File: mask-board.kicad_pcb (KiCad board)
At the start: 2 copper layers, 56.5 x 41.9 mm, 58 parts, among them J1 SWIM Connector, J2 I2C Breakout, M1 Fan_3pin, M2 Fan_3pin, M3 Motor_DC, Q1 2N7000, Q2 2N7000, Q3 2N7000, Q4 2N7000, SW1 SW_Push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

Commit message: Update to V3
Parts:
- D2, D3, D4: value D_Schottky -> PMEG4010ER; footprint Package_TO_SOT_SMD:SOT-23-3 -> Diode_SMD:Nexperia_CFP3_SOD-123W
- M1, M2: footprint Connector_PinHeader_2.54mm:PinHeader_1x03_P2.54mm_Vertical -> footprints:JST-XH-3-pin
- M3: footprint Connector_PinHeader_2.54mm:PinHeader_1x02_P2.54mm_Vertical -> footprints:JST-XH-2-pin
- Q1, Q2, Q3, Q4: value 2N7000 -> DMN10H220L; footprint Package_TO_SOT_THT:TO-92_Inline -> Package_TO_SOT_SMD:SOT-23
- moved Q2 9.75 mm to (166.4, 99.4), turned to 0 degrees
- moved R11 7.41 mm to (160.3, 104.1), turned to 90 degrees
- moved C17 5.15 mm to (170.5, 104.1)
- moved C18 5.15 mm to (166.7, 104.1)
- moved C19 5.15 mm to (168.6, 104.1)
- moved M3 4.74 mm to (174.0, 102.8), turned to 90 degrees
- moved M2 4.13 mm to (174.0, 93.0), turned to 90 degrees
- moved R10 3.62 mm to (162.2, 104.1), turned to 90 degrees
- moved M1 3.18 mm to (174.0, 81.9), turned to 90 degrees
- moved Q4 2.53 mm to (166.0, 89.2), turned to 0 degrees
- moved R14 1.94 mm to (163.8, 93.2)
- moved R15 1.94 mm to (165.7, 93.2)
- moved Q1 1.44 mm to (154.6, 96.5), turned to 0 degrees
- moved Q3 0.95 mm to (164.8, 80.3), turned to 0 degrees
- moved D2 0.55 mm to (169.9, 98.9), turned to -90 degrees
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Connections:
- Q1 pad 1: GND -> Net-(Q1-G)
- Q1 pad 2: Net-(Q1-G) -> GND
- Q2 pad 1: GND -> Net-(Q2-G)
- Q2 pad 2: Net-(Q2-G) -> GND
- Q3 pad 1: GND -> Net-(Q3-G)
- Q3 pad 2: Net-(Q3-G) -> GND
- Q4 pad 1: GND -> Net-(Q4-G)
- Q4 pad 2: Net-(Q4-G) -> GND
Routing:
- net ERM_MOTOR: track 20.1 -> 14.1 mm
- net Net-(BZ1--): track 8.40 -> 14.0 mm, vias 0 -> 1
- net +3V3: track 157.4 -> 162.9 mm
- net +5V: track 71.3 -> 74.6 mm
- net Net-(Q2-G): track 5.01 -> 7.10 mm
- net FAN_2: track 18.2 -> 20.2 mm
- net Net-(D4-A): track 9.43 -> 7.82 mm
- net Net-(D2-A): track 10.2 -> 8.65 mm
- net Net-(Q1-G): track 4.65 -> 5.88 mm
- net Net-(M2-Tacho): track 2.99 -> 3.63 mm
- net Net-(Q4-G): track 5.11 -> 4.59 mm
- net GND: track 77.4 -> 77.8 mm, vias 5 -> 8
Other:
- board size 56.5 x 41.9 mm -> 61 x 41.9 mm

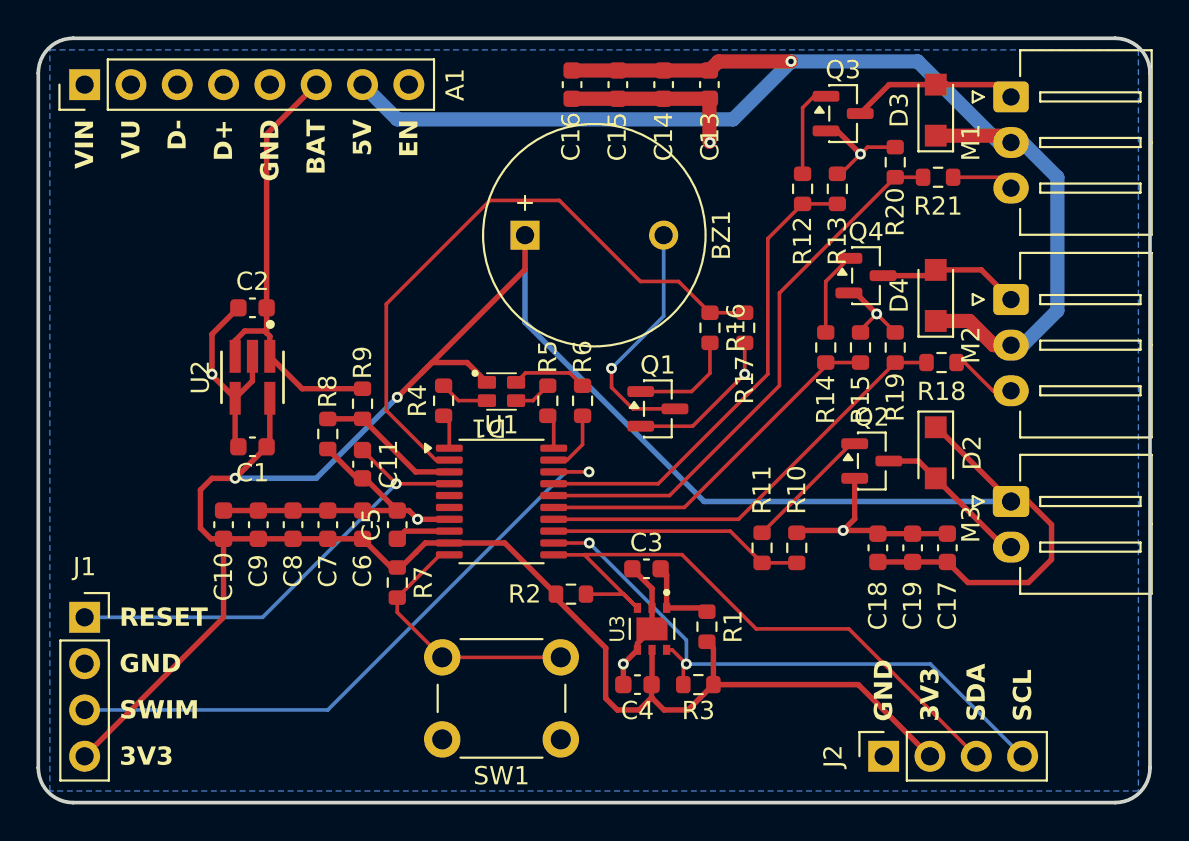
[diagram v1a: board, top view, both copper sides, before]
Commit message: Update to V4; Add quarter for scale in 3D model
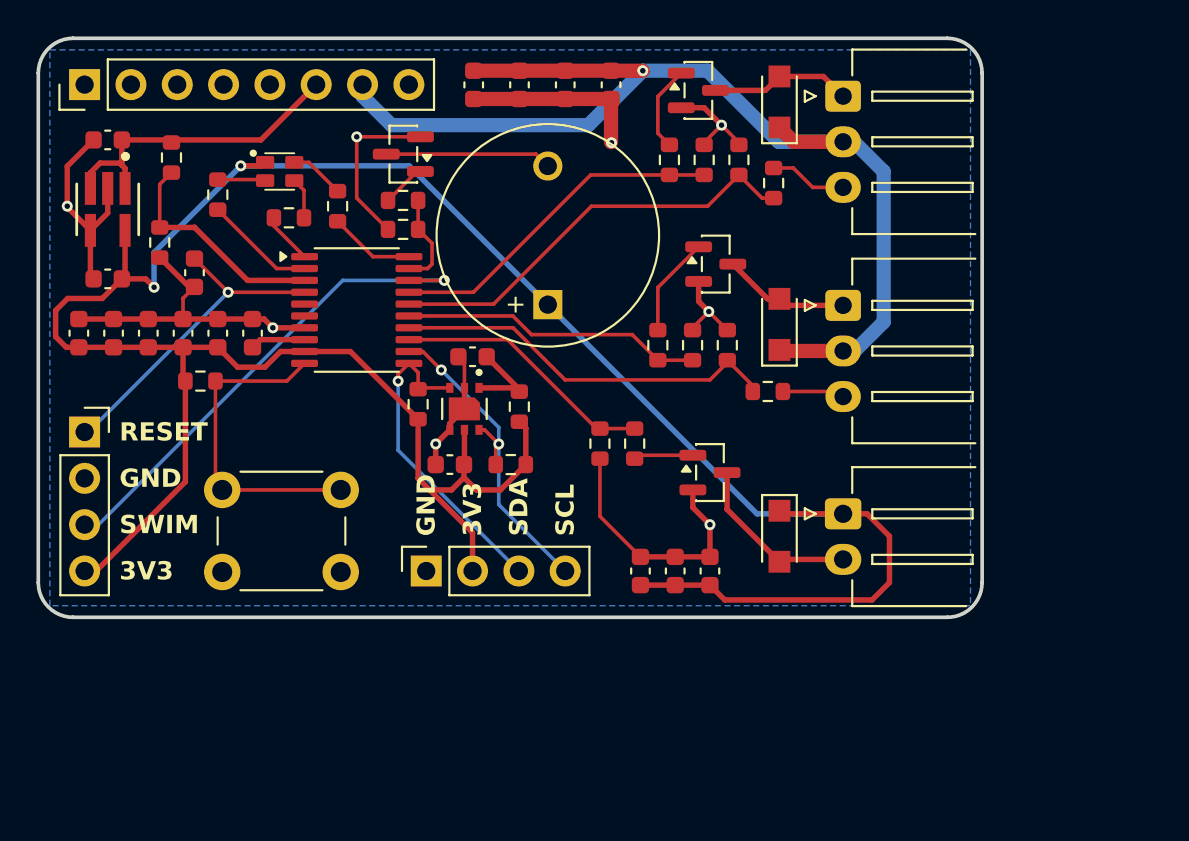
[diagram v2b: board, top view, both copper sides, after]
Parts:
- added REF**: Quarter_For_Scale, footprints:Quarter_For_Scale, F.Cu at (95.2, 92.1)
- added Ref**: Val**, footprints:logo, F.Cu at (169.2, 92.1)
- moved J2 27.1 mm to (141.9, 105.4)
- moved Q1 19.7 mm to (140.7, 82.6), turned to 180 degrees
- moved R17 19.5 mm to (140.7, 86.7), turned to 180 degrees
- moved R16 18.2 mm to (140.7, 85.1), turned to 180 degrees
- moved R5 17.4 mm to (134.4, 86.0), turned to 0 degrees
- moved R6 17.2 mm to (137.1, 85.4)
- moved D1 17.1 mm to (133.9, 83.5)
- moved R9 17.1 mm to (128.0, 82.7)
- moved R4 16.8 mm to (130.5, 84.8)
- moved C4 15.9 mm to (143.2, 99.6)
- moved R1 15.9 mm to (147.0, 96.4)
- moved R3 15.9 mm to (146.6, 99.6)
- moved U3 15.9 mm to (144.0, 96.5)
- moved R7 15.4 mm to (129.5, 95.0), turned to 0 degrees
- moved SW1 15.2 mm to (137.2, 105.5)
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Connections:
- U1 pad 1: LED_RED -> LED_GREEN
- U1 pad 19: LED_BLUE -> BUZZER
- U1 pad 2: BUZZER -> LED_RED
- U1 pad 20: LED_GREEN -> LED_BLUE
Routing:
- net BUZZER: track 35.0 -> 5.17 mm
- net +3V3: track 162.9 -> 143.0 mm
- net SDA: track 35.0 -> 17.8 mm, vias 0 -> 1
- net SCL: track 33.9 -> 18.6 mm
- net +5V: track 74.6 -> 61.1 mm
- net RESET: track 25.6 -> 17.8 mm
- net SWIM: track 35.0 -> 27.2 mm
- net FAN_1: track 26.3 -> 18.9 mm
- net +BATT: track 24.8 -> 17.5 mm
- net FAN_1_TACHO: track 30.5 -> 23.5 mm
- net Net-(BZ1--): track 14.0 -> 9.13 mm, vias 1 -> 0
- net Net-(U1-PD6): track 7.87 -> 12.4 mm
- net LED_RED: track 1.90 -> 6.09 mm
- net Net-(Q2-G): track 7.10 -> 3.27 mm
- net Net-(U1-PA3): track 14.6 -> 18.4 mm
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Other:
- board size 61 x 41.9 mm -> 51.8 x 31.8 mm
- board text removed: "5V"
- board text removed: "BAT"
- board text removed: "D+"
- board text removed: "D-"
- board text removed: "EN"
- board text removed: "VIN"
- board text removed: "VU"

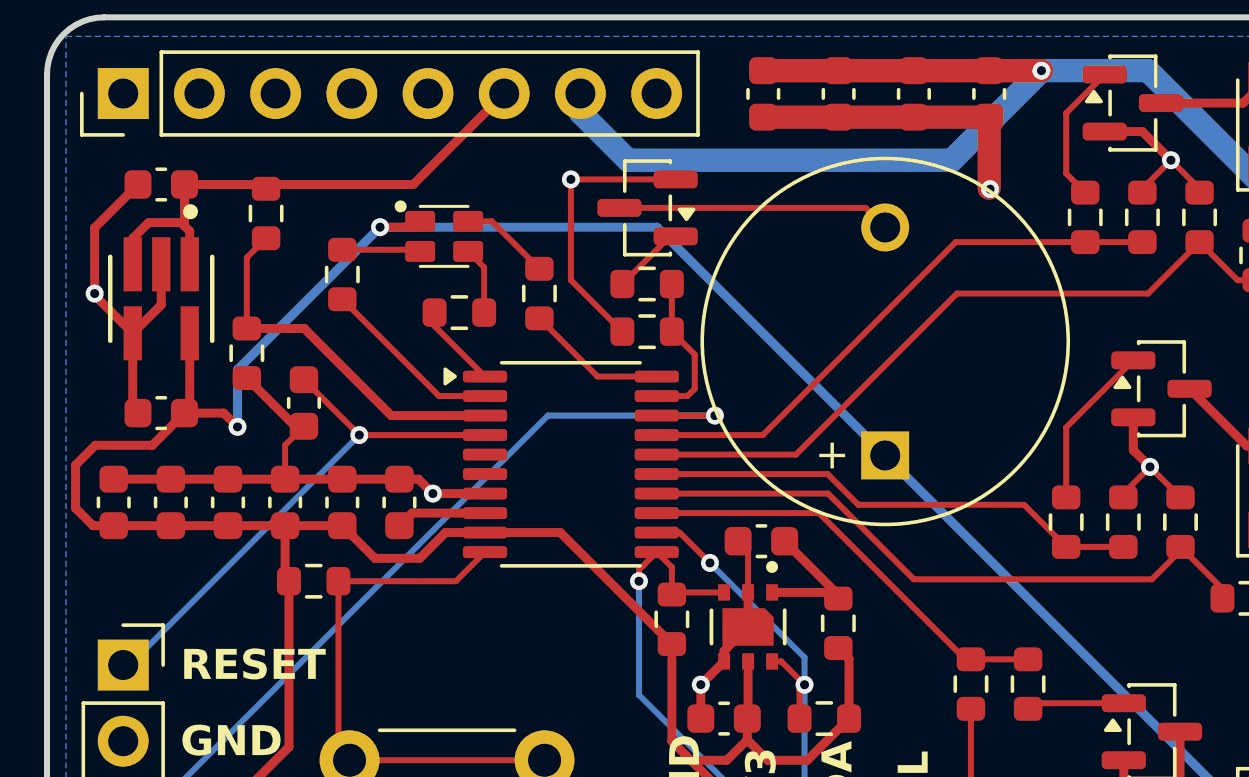
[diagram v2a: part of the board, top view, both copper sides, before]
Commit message: Fix trace width and cleanup redundant traces
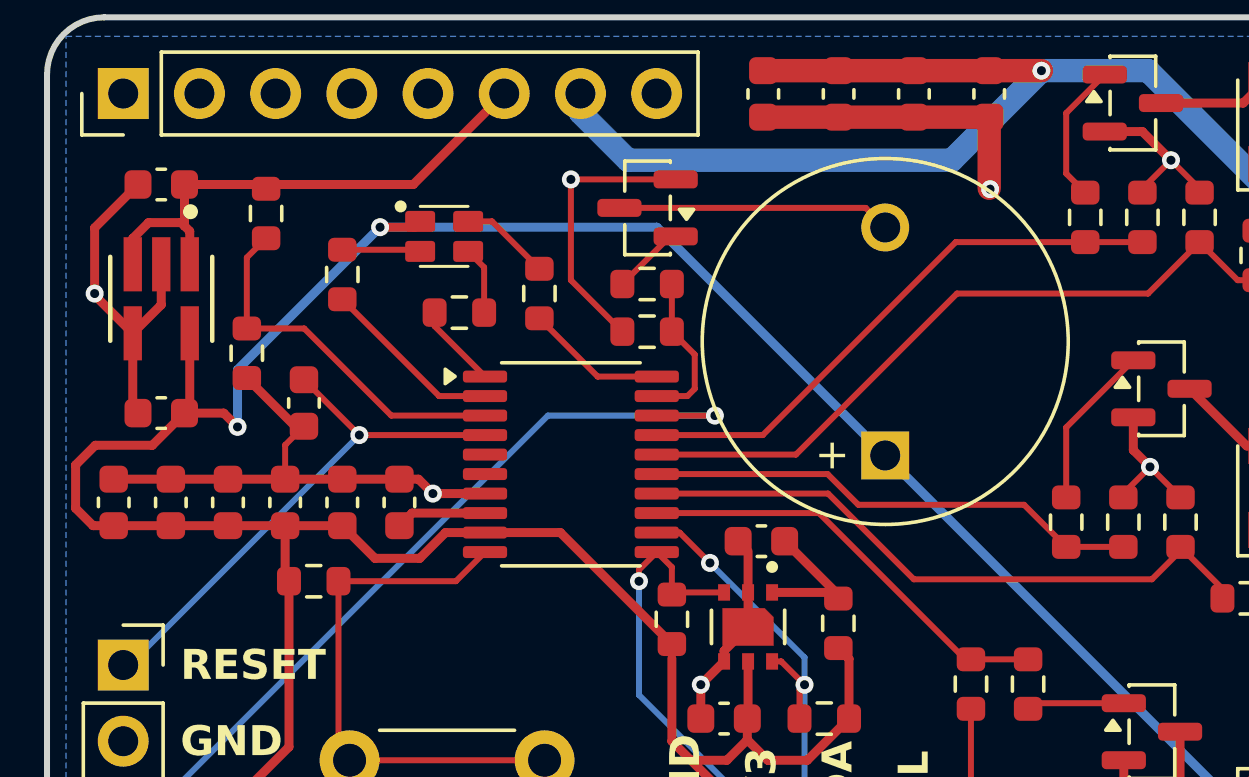
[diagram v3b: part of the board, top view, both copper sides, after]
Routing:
- net Net-(U1-PA3): track 18.4 -> 17.9 mm
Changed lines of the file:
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@@
 	)
 	(segment
-		(start 125.232501 82.930603)
+		(start 125.232501 83.154399)
 		(end 125.232501 81.772501)
 		(width 0.3)
@@
 		(start 125.232501 81.772501)
 		(end 132.857499 81.772501)
-		(width 0.3)
-		(layer "F.Cu")
-		(net 1)
-	)
-	(segment
-		(start 125.232501 82.930603)
-		(end 125.232501 83.154399)
 		(width 0.3)
 		(layer "F.Cu")
@@
 	)
 	(segment
-		(start 129.215 89.83)
-		(end 129.355 89.83)
-		(width 0.3)
-		(layer "F.Cu")
-		(net 6)
-	)
-	(segment
 		(start 127.31 88.2225)
 		(end 128.9175 89.83)
@@
 		(start 144.018 93.993)
 		(end 144.018 95.37)
-		(width 0.2)
+		(width 0.3)
 		(layer "F.Cu")
 		(net 6)
@@
 	)
 	(segment
-		(start 135.25 88.175)
-		(end 135.0675 88.175)
-		(width 0.2)
-		(layer "F.Cu")
-		(net 30)
-	)
-	(segment
 		(start 133.57 86.0425)
 		(end 133.57 86.495)
@@
 	)
 	(segment
-		(start 154.6225 93.8525)
-		(end 154.6225 94.0425)
-		(width 0.2)
-		(layer "F.Cu")
-		(net 34)
-	)
-	(segment
 		(start 146.67 91.425)
 		(end 140.975 91.425)
@@
 	)
 	(segment
+		(start 127.31 84.2075)
+		(end 127.9525 83.565)
+		(width 0.2)
+		(layer "F.Cu")
+		(net 39)
+	)
+	(segment
+		(start 129.2225 86.5725)
+		(end 127.31 86.5725)
+		(width 0.2)
+		(layer "F.Cu")
+		(net 39)
+	)
+	(segment
+		(start 127.31 86.5725)
+		(end 127.31 84.2075)
+		(width 0.2)
+		(layer "F.Cu")
+		(net 39)
+	)
+	(segment
 		(start 135.25 89.475)
 		(end 132.125 89.475)
-		(width 0.3)
+		(width 0.2)
 		(layer "F.Cu")
 		(net 39)
@@
 	(segment
 		(start 132.125 89.475)
-		(end 129.215 86.565)
-		(width 0.3)
-		(layer "F.Cu")
-		(net 39)
-	)
-	(segment
-		(start 129.2075 86.5725)
-		(end 127.31 86.5725)
-		(width 0.3)
-		(layer "F.Cu")
-		(net 39)
-	)
-	(segment
-		(start 129.215 86.565)
-		(end 129.2075 86.5725)
-		(width 0.3)
-		(layer "F.Cu")
-		(net 39)
-	)
-	(segment
-		(start 127.31 84.2075)
-		(end 127.9525 83.565)
-		(width 0.2)
-		(layer "F.Cu")
-		(net 39)
-	)
-	(segment
-		(start 127.31 86.5725)
-		(end 127.31 84.2075)
+		(end 129.2225 86.5725)
 		(width 0.2)
 		(layer "F.Cu")
@@
 		(width 0.2)
 		(layer "F.Cu")
-		(net 40)
-	)
-	(segment
-		(start 135.25 94.075)
-		(end 134.7425 94.075)
-		(width 0.2)
-		(layer "F.Cu")

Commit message: Generate gerbers
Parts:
- A1: moved to B.Cu
- turned A1 to -90 degrees
